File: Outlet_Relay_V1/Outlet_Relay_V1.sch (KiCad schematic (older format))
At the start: 7 parts

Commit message: Added footprints to resistors.
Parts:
- R? (x2): footprint (none) -> Resistor_SMD:R_0603_1608Metric_Pad1.05x0.95mm_HandSolder
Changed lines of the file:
@@
 EESchema Schematic File Version 4
+LIBS:Outlet_Relay_V1-cache
 EELAYER 26 0
 EELAYER END
@@
 F 0 "R?" H 4545 3521 50  0000 L CNN
 F 1 "1k" H 4545 3430 50  0000 L CNN
-F 2 "" V 4405 3475 50  0001 C CNN
+F 2 "Resistor_SMD:R_0603_1608Metric_Pad1.05x0.95mm_HandSolder" V 4405 3475 50  0001 C CNN
 F 3 "~" H 4475 3475 50  0001 C CNN
 	1    4475 3475
@@
 F 0 "R?" H 4720 3996 50  0000 L CNN
 F 1 "10k" H 4720 3905 50  0000 L CNN
-F 2 "" V 4580 3950 50  0001 C CNN
+F 2 "Resistor_SMD:R_0603_1608Metric_Pad1.05x0.95mm_HandSolder" V 4580 3950 50  0001 C CNN
 F 3 "~" H 4650 3950 50  0001 C CNN
 	1    4650 3950

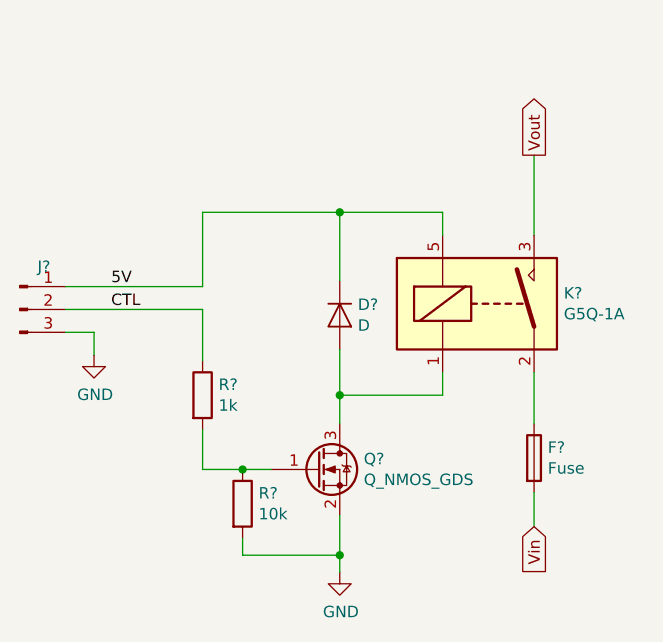
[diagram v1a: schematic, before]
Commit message: Finished PCB layout. Generated BOM.
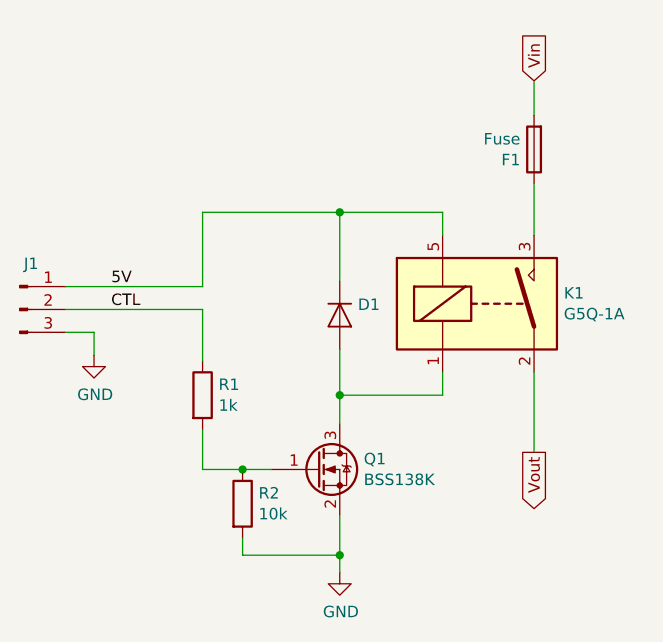
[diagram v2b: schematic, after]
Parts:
- D1: renamed from D?; value D -> BAS116H,115; footprint (none) -> Diode_SMD:D_SOD-123F
- F1: renamed from F?; footprint (none) -> Custom_Footprints:Fuse_Holder_Keystone_4527_Cartridge
- J1: renamed from J?; value Conn_01x03_Male -> TerminalBlock_1x3_5.08mmPitch; footprint (none) -> Custom_Footprints:TerminalBlock_Molex_1x3_5.04mmPitch
- Q1: renamed from Q?; value Q_NMOS_GDS -> BSS138K; footprint (none) -> Package_TO_SOT_SMD:SOT-23_Handsoldering
- gave numbers to parts that had none: 3
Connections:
- net Vout: now also K1.2; no longer K1.3
- net at F1.1: now also K1.3; no longer K1.2
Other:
- moved on the sheet: F1
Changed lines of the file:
@@
 $EndDescr
 $Comp
-L Relay:G5Q-1A K?
+L Relay:G5Q-1A K1
 U 1 1 5C25CF2F
 P 5725 3075
-F 0 "K?" H 6055 3121 50  0000 L CNN
+F 0 "K1" H 6055 3121 50  0000 L CNN
 F 1 "G5Q-1A" H 6055 3030 50  0000 L CNN
 F 2 "Relay_THT:Relay_SPST_Omron-G5Q-1A" H 6075 3025 50  0001 L CNN
@@
 $EndComp
 $Comp
-L Device:Fuse F?
+L Device:Fuse F1
 U 1 1 5C25D06C
-P 5925 3750
-F 0 "F?" H 5985 3796 50  0000 L CNN
-F 1 "Fuse" H 5985 3705 50  0000 L CNN
-F 2 "" V 5855 3750 50  0001 C CNN
-F 3 "~" H 5925 3750 50  0001 C CNN
-	1    5925 3750
-	1    0    0    -1
+P 5925 2400
+F 0 "F1" H 5985 2446 50  0000 L CNN
+F 1 "Fuse" H 5985 2355 50  0000 L CNN
+F 2 "Custom_Footprints:Fuse_Holder_Keystone_4527_Cartridge" V 5855 2400 50  0001 C CNN
+F 3 "~" H 5925 2400 50  0001 C CNN
+	1    5925 2400
+	-1   0    0    1
 $EndComp
 $Comp
-L Connector:Conn_01x03_Male J?
+L Connector:Conn_01x03_Male J1
 U 1 1 5C25D1DC
 P 3675 3100
-F 0 "J?" H 3781 3287 50  0000 C CNN
-F 1 "Conn_01x03_Male" H 3781 3287 50  0001 C CNN
-F 2 "" H 3675 3100 50  0001 C CNN
+F 0 "J1" H 3725 3300 50  0000 C CNN
+F 1 "TerminalBlock_1x3_5.08mmPitch" H 3781 3287 50  0001 C CNN
+F 2 "Custom_Footprints:TerminalBlock_Molex_1x3_5.04mmPitch" H 3675 3100 50  0001 C CNN
 F 3 "~" H 3675 3100 50  0001 C CNN
 	1    3675 3100
@@
 $EndComp
 $Comp
-L Device:Q_NMOS_GSD Q?
+L Device:Q_NMOS_GSD Q1
 U 1 1 5C25D3BE
 P 4975 3800
-F 0 "Q?" H 5180 3846 50  0000 L CNN
-F 1 "Q_NMOS_GDS" H 5180 3755 50  0000 L CNN
-F 2 "" H 5175 3900 50  0001 C CNN
+F 0 "Q1" H 5180 3846 50  0000 L CNN
+F 1 "BSS138K" H 5180 3755 50  0000 L CNN
+F 2 "Package_TO_SOT_SMD:SOT-23_Handsoldering" H 5175 3900 50  0001 C CNN
 F 3 "~" H 4975 3800 50  0001 C CNN
 	1    4975 3800
@@
 $EndComp
 $Comp
-L Device:D D?
+L Device:D D1
 U 1 1 5C25D578
 P 5075 3125
-F 0 "D?" V 5029 3204 50  0000 L CNN
-F 1 "D" V 5120 3204 50  0000 L CNN
-F 2 "" H 5075 3125 50  0001 C CNN
+F 0 "D1" V 5029 3204 50  0000 L CNN
+F 1 "BAS116H,115" V 5120 3204 50  0001 L CNN
+F 2 "Diode_SMD:D_SOD-123F" H 5075 3125 50  0001 C CNN
 F 3 "~" H 5075 3125 50  0001 C CNN
 	1    5075 3125
@@
 $EndComp
 $Comp
-L power:GND #PWR?
+L power:GND #PWR01
 U 1 1 5C25DCF3
 P 4000 3300
-F 0 "#PWR?" H 4000 3050 50  0001 C CNN
+F 0 "#PWR01" H 4000 3050 50  0001 C CNN
 F 1 "GND" H 4005 3127 50  0000 C CNN
 F 2 "" H 4000 3300 50  0001 C CNN
@@
 $EndComp
 $Comp
-L power:GND #PWR?
+L power:GND #PWR02
 U 1 1 5C25DD0F
 P 5075 4250
-F 0 "#PWR?" H 5075 4000 50  0001 C CNN
+F 0 "#PWR02" H 5075 4000 50  0001 C CNN
 F 1 "GND" H 5080 4077 50  0000 C CNN
 F 2 "" H 5075 4250 50  0001 C CNN
@@
 	3875 3100 4475 3100
 Wire Wire Line
-	5925 3600 5925 3375
+	5925 2550 5925 2775
 Wire Wire Line
-	5925 2775 5925 2425
+	5925 3375 5925 3725
 Wire Wire Line
-	5925 3900 5925 4050
+	5925 2250 5925 2100
 Wire Wire Line
 	3875 3000 4475 3000
-Text GLabel 5925 4050 3    50   Input ~ 0
+Text GLabel 5925 2100 1    50   Input ~ 0
 Vin
-Text GLabel 5925 2425 1    50   Output ~ 0
+Text GLabel 5925 3725 3    50   Output ~ 0
 Vout
 Text Label 4075 3000 0    50   ~ 0
@@
 CTL
 $Comp
-L Device:R R?
+L Device:R R1
 U 1 1 5C25E7B9
 P 4475 3475
-F 0 "R?" H 4545 3521 50  0000 L CNN
+F 0 "R1" H 4545 3521 50  0000 L CNN
 F 1 "1k" H 4545 3430 50  0000 L CNN
 F 2 "Resistor_SMD:R_0603_1608Metric_Pad1.05x0.95mm_HandSolder" V 4405 3475 50  0001 C CNN
@@
 $EndComp
 $Comp
-L Device:R R?
+L Device:R R2
 U 1 1 5C25E85D
 P 4650 3950
-F 0 "R?" H 4720 3996 50  0000 L CNN
+F 0 "R2" H 4720 3996 50  0000 L CNN
 F 1 "10k" H 4720 3905 50  0000 L CNN
 F 2 "Resistor_SMD:R_0603_1608Metric_Pad1.05x0.95mm_HandSolder" V 4580 3950 50  0001 C CNN
